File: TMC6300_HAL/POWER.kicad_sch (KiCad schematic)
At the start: 23 parts, among them IC301 MP1479GTF-Z, IC302 MP1479GTF-Z

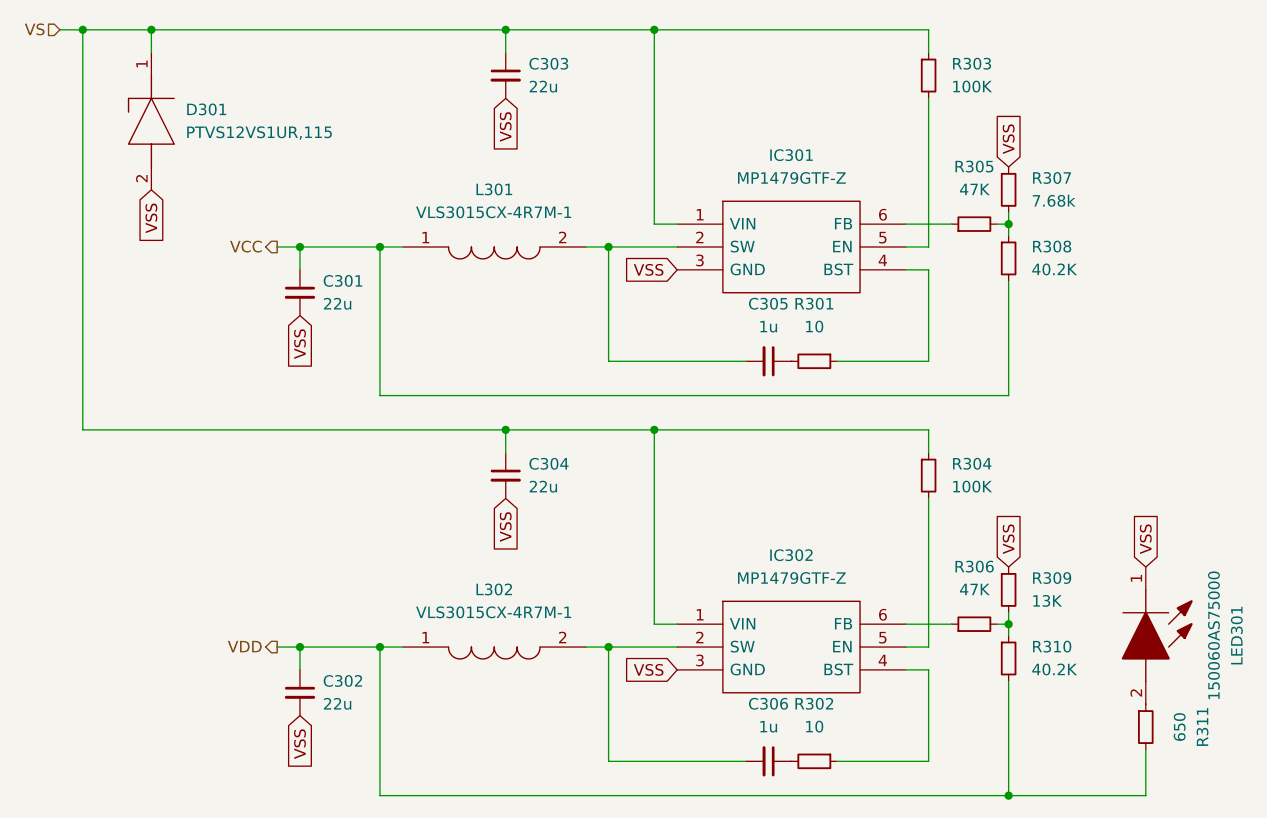
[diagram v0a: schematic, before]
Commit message: Version used with Lencon blower.
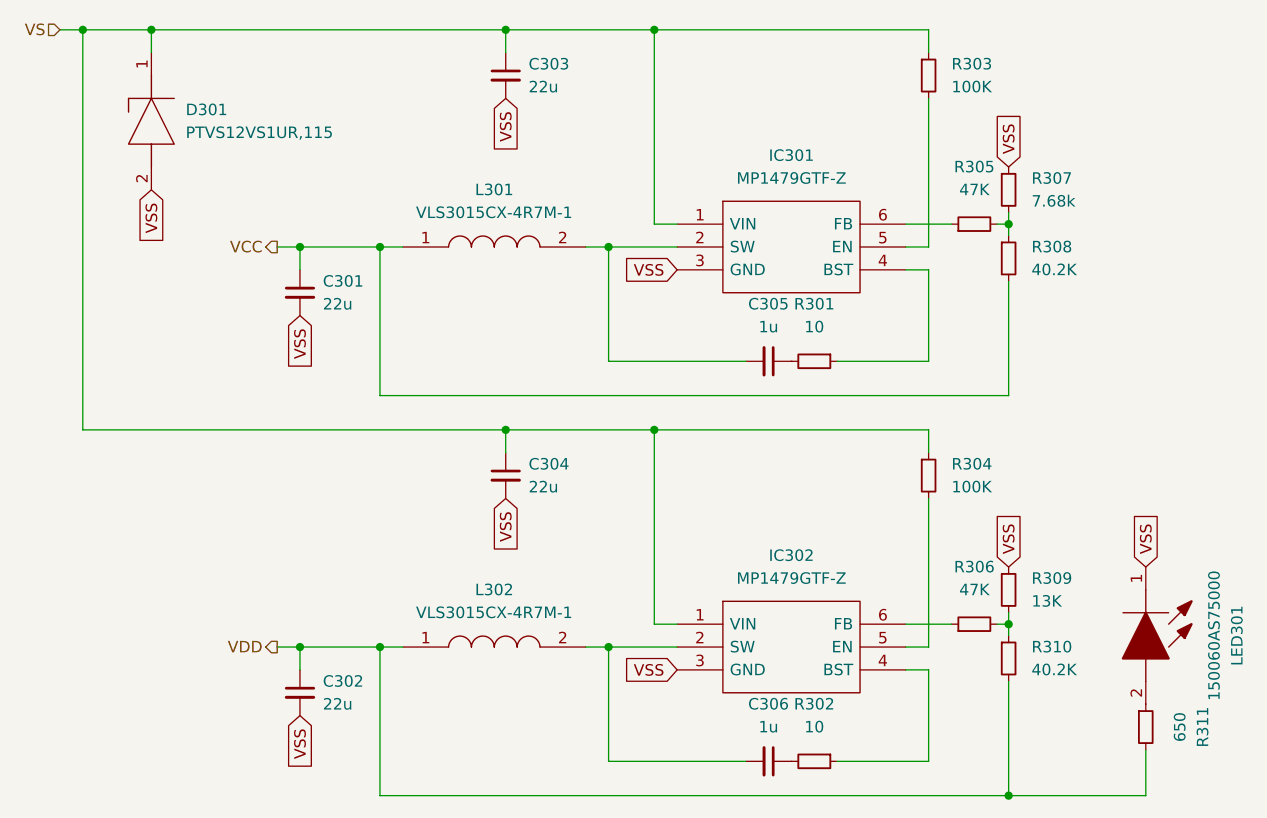
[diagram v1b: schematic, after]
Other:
- moved on the sheet: L301, L302
